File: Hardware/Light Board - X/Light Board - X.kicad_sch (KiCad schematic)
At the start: 11 parts, among them J1 V+, J2 V-

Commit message: Added production file generation tools
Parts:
- D1, D2, D3, D4, D5, D6, D7, D8, D9: DigiKey PN (none) -> 2138-JB2835AWT-W-H40GA0000-N0000001CT-ND; LCSC PN C385299 -> (none); MPN 67-21S/KK5C-H402633Z6/2T(CLW) -> JB2835AWT-W-H40GA0000-N0000001
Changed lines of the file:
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@@
 			)
 		)
-		(property "MPN" "67-21S/KK5C-H402633Z6/2T(CLW)"
+		(property "MPN" "JB2835AWT-W-H40GA0000-N0000001"
 			(at 113.03 168.91 90)
 			(effects
@@
 			)
 		)
-		(property "LCSC PN" "C385299"
+		(property "LCSC PN" ""
+			(at 113.03 168.91 90)
+			(effects
+				(font
+					(size 1.27 1.27)
+				)
+				(hide yes)
+			)
+		)
+		(property "DigiKey PN" "2138-JB2835AWT-W-H40GA0000-N0000001CT-ND"
 			(at 113.03 168.91 90)
 			(effects
@@
 			)
 		)
-		(property "MPN" "67-21S/KK5C-H402633Z6/2T(CLW)"
+		(property "MPN" "JB2835AWT-W-H40GA0000-N0000001"
 			(at 113.03 158.75 90)
 			(effects
@@
 			)
 		)
-		(property "LCSC PN" "C385299"
+		(property "LCSC PN" ""
+			(at 113.03 158.75 90)
+			(effects
+				(font
+					(size 1.27 1.27)
+				)
+				(hide yes)
+			)
+		)
+		(property "DigiKey PN" "2138-JB2835AWT-W-H40GA0000-N0000001CT-ND"
 			(at 113.03 158.75 90)
 			(effects
@@
 			)
 		)
-		(property "MPN" "67-21S/KK5C-H402633Z6/2T(CLW)"
+		(property "MPN" "JB2835AWT-W-H40GA0000-N0000001"
 			(at 113.03 128.27 90)
 			(effects
@@
 			)
 		)
-		(property "LCSC PN" "C385299"
+		(property "LCSC PN" ""
+			(at 113.03 128.27 90)
+			(effects
+				(font
+					(size 1.27 1.27)
+				)
+				(hide yes)
+			)
+		)
+		(property "DigiKey PN" "2138-JB2835AWT-W-H40GA0000-N0000001CT-ND"
 			(at 113.03 128.27 90)
 			(effects
@@
 			)
 		)
-		(property "MPN" "67-21S/KK5C-H402633Z6/2T(CLW)"
+		(property "MPN" "JB2835AWT-W-H40GA0000-N0000001"
 			(at 113.03 97.79 90)
 			(effects
@@
 			)
 		)
-		(property "LCSC PN" "C385299"
+		(property "LCSC PN" ""
+			(at 113.03 97.79 90)
+			(effects
+				(font
+					(size 1.27 1.27)
+				)
+				(hide yes)
+			)
+		)
+		(property "DigiKey PN" "2138-JB2835AWT-W-H40GA0000-N0000001CT-ND"
 			(at 113.03 97.79 90)
 			(effects
@@
 			)
 		)
-		(property "MPN" "67-21S/KK5C-H402633Z6/2T(CLW)"
+		(property "MPN" "JB2835AWT-W-H40GA0000-N0000001"
 			(at 113.03 138.43 90)
 			(effects
@@
 			)
 		)
-		(property "LCSC PN" "C385299"
+		(property "LCSC PN" ""
+			(at 113.03 138.43 90)
+			(effects
+				(font
+					(size 1.27 1.27)
+				)
+				(hide yes)
+			)
+		)
+		(property "DigiKey PN" "2138-JB2835AWT-W-H40GA0000-N0000001CT-ND"
 			(at 113.03 138.43 90)
 			(effects
@@
 			)
 		)
-		(property "MPN" "67-21S/KK5C-H402633Z6/2T(CLW)"
+		(property "MPN" "JB2835AWT-W-H40GA0000-N0000001"
 			(at 113.03 148.59 90)
 			(effects
@@
 			)
 		)
-		(property "LCSC PN" "C385299"
+		(property "LCSC PN" ""
+			(at 113.03 148.59 90)
+			(effects
+				(font
+					(size 1.27 1.27)
+				)
+				(hide yes)
+			)
+		)
+		(property "DigiKey PN" "2138-JB2835AWT-W-H40GA0000-N0000001CT-ND"
 			(at 113.03 148.59 90)
 			(effects
@@
 			)
 		)
-		(property "MPN" "67-21S/KK5C-H402633Z6/2T(CLW)"
+		(property "MPN" "JB2835AWT-W-H40GA0000-N0000001"
 			(at 113.03 107.95 90)
 			(effects
@@
 			)
 		)
-		(property "LCSC PN" "C385299"
+		(property "LCSC PN" ""
+			(at 113.03 107.95 90)
+			(effects
+				(font
+					(size 1.27 1.27)
+				)
+				(hide yes)
+			)
+		)
+		(property "DigiKey PN" "2138-JB2835AWT-W-H40GA0000-N0000001CT-ND"
 			(at 113.03 107.95 90)
 			(effects
@@
 			)
 		)
+		(property "DigiKey PN" ""
+			(at 100.33 78.74 0)
+			(effects
+				(font
+					(size 1.27 1.27)
+				)
+				(hide yes)
+			)
+		)
 		(pin "1"
 		)
@@
 			)
 		)
-		(property "MPN" "67-21S/KK5C-H402633Z6/2T(CLW)"
+		(property "MPN" "JB2835AWT-W-H40GA0000-N0000001"
 			(at 113.03 118.11 90)
 			(effects
@@
 			)
 		)
-		(property "LCSC PN" "C385299"
+		(property "LCSC PN" ""
+			(at 113.03 118.11 90)
+			(effects
+				(font
+					(size 1.27 1.27)
+				)
+				(hide yes)
+			)
+		)
+		(property "DigiKey PN" "2138-JB2835AWT-W-H40GA0000-N0000001CT-ND"
 			(at 113.03 118.11 90)
 			(effects
@@
 			)
 		)
+		(property "DigiKey PN" ""
+			(at 100.33 179.07 0)
+			(effects
+				(font
+					(size 1.27 1.27)
+				)
+				(hide yes)
+			)
+		)
 		(pin "1"
 		)
@@
 			)
 		)
-		(property "MPN" "67-21S/KK5C-H402633Z6/2T(CLW)"
+		(property "MPN" "JB2835AWT-W-H40GA0000-N0000001"
 			(at 113.03 87.63 90)
 			(effects
@@
 			)
 		)
-		(property "LCSC PN" "C385299"
+		(property "LCSC PN" ""
 			(at 113.03 87.63 90)
 			(effects
+				(font
+					(size 1.27 1.27)
+				)
+				(hide yes)
+			)
+		)
+		(property "DigiKey PN" "2138-JB2835AWT-W-H40GA0000-N0000001CT-ND"
+			(at 113.03 87.63 90)
+			(effects

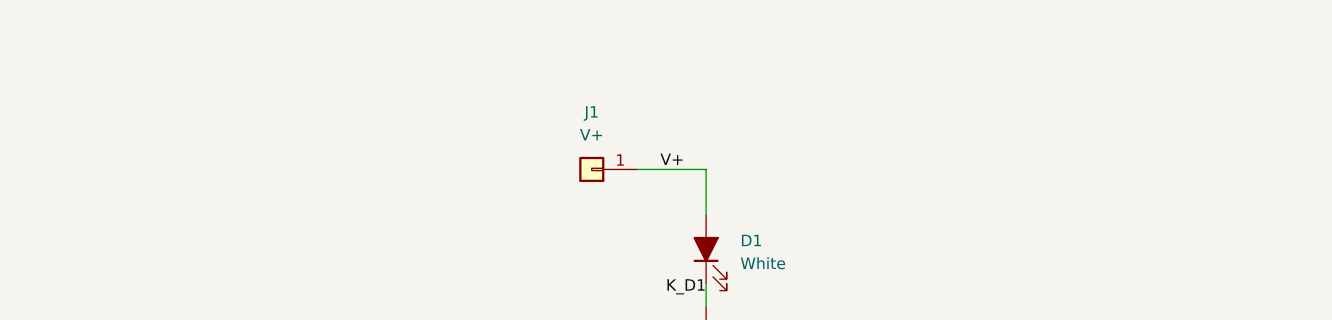
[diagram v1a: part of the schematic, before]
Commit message: Added note about incorrect footprint orientation
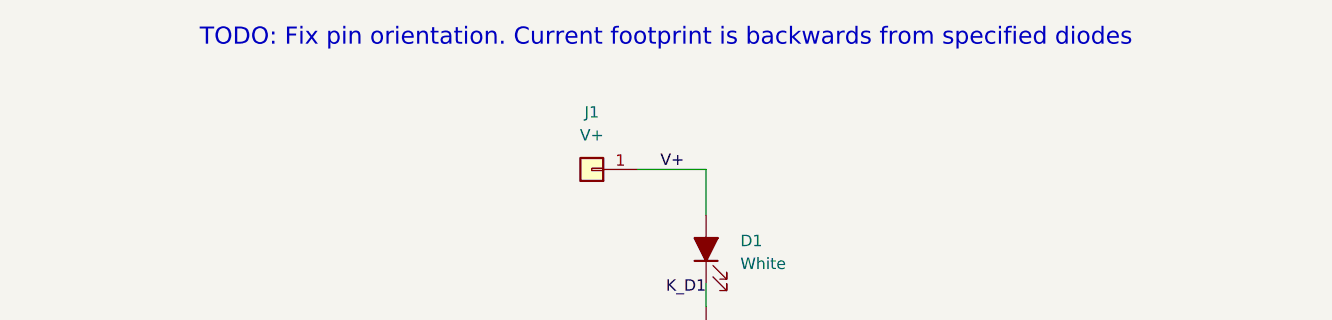
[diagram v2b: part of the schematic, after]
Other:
- note added: "TODO: Fix pin orientation. Current footprint is backwards from specified diodes"
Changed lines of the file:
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@@
 		(comment 1 "Isaac Rex")
+	)
+	(text "TODO: Fix pin orientation. Current footprint is backwards from specified diodes"
+		(exclude_from_sim no)
+		(at 108.585 64.135 0)
+		(effects
+			(font
+				(size 1.905 1.905)
+			)
+		)
 	)
 	(wire

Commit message: Added LED library and fixed orientation
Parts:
- D1: renamed from D9; footprint LED_SMD:LED_Everlight-SMD3528_3.5x2.8mm_67-21ST -> irex_LED_SMD:LED_Cree_J-Series_SMD2835_2.8x3.5mm
- D2: renamed from D8; footprint LED_SMD:LED_Everlight-SMD3528_3.5x2.8mm_67-21ST -> irex_LED_SMD:LED_Cree_J-Series_SMD2835_2.8x3.5mm
- D3: renamed from D7; footprint LED_SMD:LED_Everlight-SMD3528_3.5x2.8mm_67-21ST -> irex_LED_SMD:LED_Cree_J-Series_SMD2835_2.8x3.5mm
- D4: renamed from D6; footprint LED_SMD:LED_Everlight-SMD3528_3.5x2.8mm_67-21ST -> irex_LED_SMD:LED_Cree_J-Series_SMD2835_2.8x3.5mm
- D5: footprint LED_SMD:LED_Everlight-SMD3528_3.5x2.8mm_67-21ST -> irex_LED_SMD:LED_Cree_J-Series_SMD2835_2.8x3.5mm
- D6: renamed from D4; footprint LED_SMD:LED_Everlight-SMD3528_3.5x2.8mm_67-21ST -> irex_LED_SMD:LED_Cree_J-Series_SMD2835_2.8x3.5mm
- D7: renamed from D3; footprint LED_SMD:LED_Everlight-SMD3528_3.5x2.8mm_67-21ST -> irex_LED_SMD:LED_Cree_J-Series_SMD2835_2.8x3.5mm
- D8: renamed from D2; footprint LED_SMD:LED_Everlight-SMD3528_3.5x2.8mm_67-21ST -> irex_LED_SMD:LED_Cree_J-Series_SMD2835_2.8x3.5mm
- D9: renamed from D1; footprint LED_SMD:LED_Everlight-SMD3528_3.5x2.8mm_67-21ST -> irex_LED_SMD:LED_Cree_J-Series_SMD2835_2.8x3.5mm
- J1: renamed from J2; value V- -> V+
- J2: renamed from J1; value V+ -> V-
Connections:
- net K_D1: now also D1.1 (K), D2.2 (A); no longer D8.2 (A), D9.1 (K)
- net K_D2: now also D2.1 (K), D3.2 (A); no longer D7.2 (A), D8.1 (K)
- net K_D3: now also D3.1 (K), D4.2 (A); no longer D6.2 (A), D7.1 (K)
- net K_D4: now also D4.1 (K); no longer D6.1 (K)
- net K_D5: now also D6.2 (A); no longer D4.2 (A)
- net K_D6: now also D6.1 (K), D7.2 (A); no longer D3.2 (A), D4.1 (K)
- net K_D7: now also D7.1 (K), D8.2 (A); no longer D2.2 (A), D3.1 (K)
- net V+: now also D1.2 (A), J1.1 (Pin_1); no longer D9.2 (A), J2.1 (Pin_1)
- net V-: now also D9.1 (K), J2.1 (Pin_1); no longer D1.1 (K), J1.1 (Pin_1)
- removed net K_D9: D1.2 (A), D2.1 (K)
- new net K_D8: D8.1 (K), D9.2 (A)
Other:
- note removed: "TODO: Fix pin orientation. Current footprint is backwards from specified diodes"
- title: Xbox Sign Light Board – X -> ${PROJECTNAME}
- moved on the sheet: D1, D2, D3, D4, D6, D7, D8, D9, J1, J2
